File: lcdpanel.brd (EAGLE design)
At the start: 90 x 65 mm, 28 parts, among them CON1 AVRISP-NEWSYMBOL-ML6, J1 CHARLCD-LONG, SW1 PUSHSW, SW2 PUSHSW, SW3 PUSHSW, SW4 PUSHSW, U1 ATTINY2313P

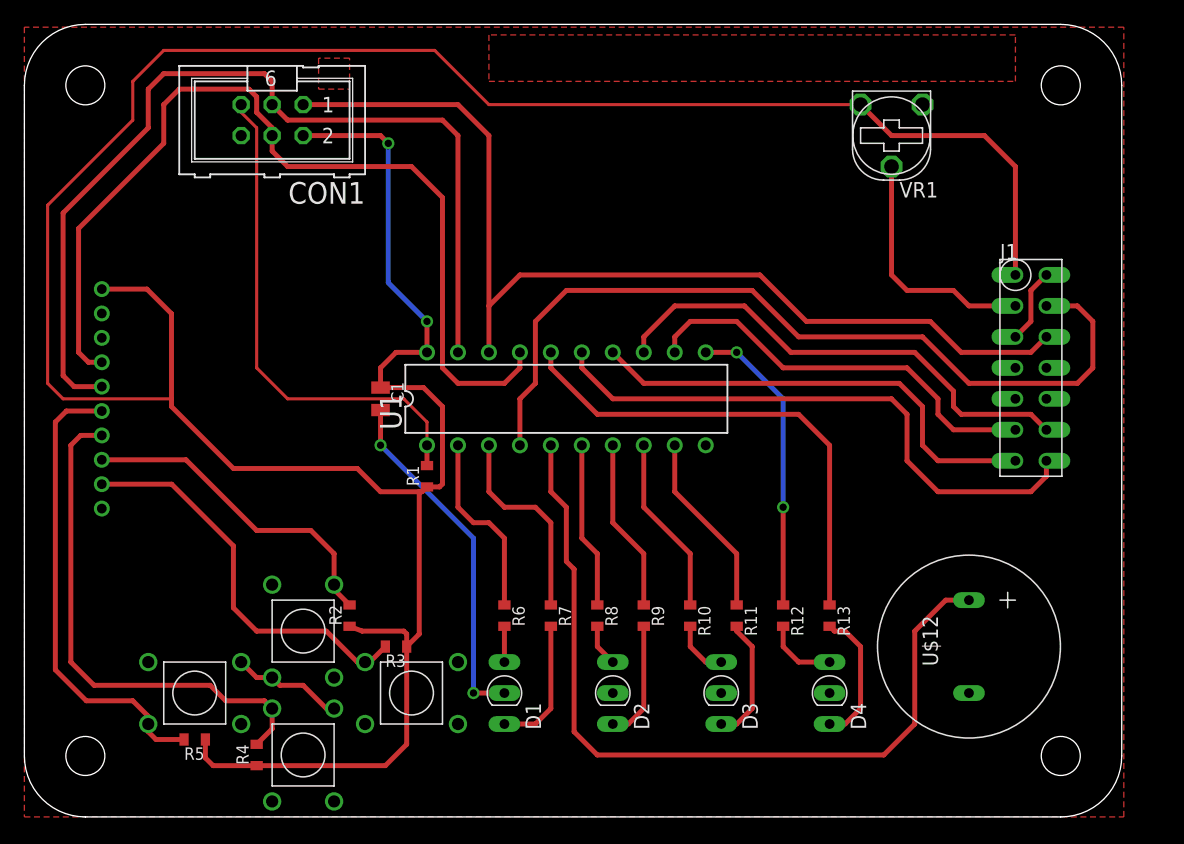
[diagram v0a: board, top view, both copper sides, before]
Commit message: added top board (ontheway)
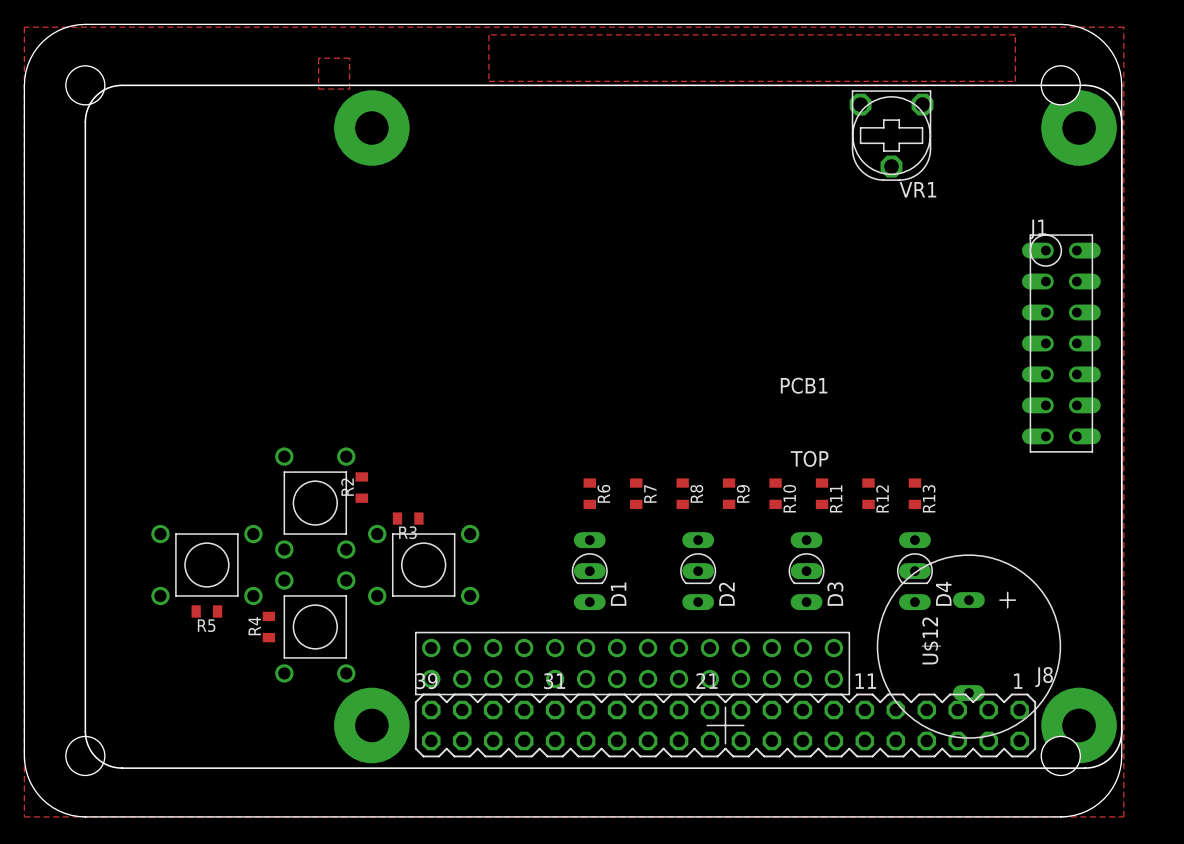
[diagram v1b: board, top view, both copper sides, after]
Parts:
- removed C1: 0.1u, Passive_Robotech:2012-C
- removed CON1: AVRISP-NEWSYMBOL-ML6, Connector_Robotech:ML6
- removed R1: 10k, Passive_Robotech:1608
- removed S1: 10B-PH, con-jst:S10B-PH
- removed U1: ATTINY2313P, MicroControler_Robotech:DIL20
- added PCB1: RASPBERRY_PI_B+, RASPBERRY_PI_Bplus:RASPBERRY_PI_B+
- added U$13: CON_14X2, pizaid:CON_14X2
- moved D3 12.2 mm to (64.2, 20.2)
- moved R12 12.2 mm to (69.2, 26.5)
- moved D1 12.2 mm to (46.4, 20.2)
- moved D2 12.2 mm to (55.3, 20.2)
- moved D4 12.2 mm to (73.0, 20.2)
- moved R10 12.2 mm to (61.6, 26.5)
- moved R11 12.2 mm to (65.4, 26.5)
- moved R13 12.2 mm to (73.0, 26.5)
- moved R6 12.2 mm to (46.4, 26.5)
- moved R7 12.2 mm to (50.2, 26.5)
- moved R8 12.2 mm to (54.0, 26.5)
- moved R9 12.2 mm to (57.8, 26.5)
- moved R5 10.5 mm to (15.0, 16.9)
- moved R2 10.5 mm to (27.7, 27.0)
- moved R4 10.5 mm to (20.1, 15.6)
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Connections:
- removed net +3V3: S1.P$2
- removed net N$12: R6.1, U1.2
- removed net N$13: R7.1, U1.3
- removed net N$14: R8.1, U1.6
- removed net N$15: R9.1, U1.7
- removed net N$16: R10.1, U1.8
- removed net N$17: R11.1, U1.9
- removed net N$18: R12.1, U1.11
- removed net N$19: R13.1, U1.16
- removed net N$20: U$12.+, U1.5
- removed net SCL: CON1.3, S1.P$5, U1.19
- removed net SDA: CON1.4, S1.P$4, U1.17
- new net LED1G: R6.1
- net +5V: now also U$13.P$5; no longer C1.1, CON1.2, R1.1, S1.P$1, U1.20
- net DB4: now also U$13.P$28; no longer U1.12
- net DB5: now also U$13.P$26; no longer U1.13
- net DB6: now also U$13.P$24; no longer U1.14
- net DB7: now also U$13.P$20; no longer U1.15
- net D_BUTTON: no longer S1.P$7
- net E: now also U$13.P$16; no longer CON1.1, U1.18
- net GND: now also U$12.+, U$13.P$13, U$13.P$18, U$13.P$2, U$13.P$22, U$13.P$27, U$13.P$8; no longer C1.2, CON1.6, S1.P$3, U$12.-, U1.10
- net L_BUTTON: no longer S1.P$6
- net N$1: now also U$12.-, U$13.P$10; no longer CON1.5, R1.2, U1.1
- net RS: now also U$13.P$14; no longer U1.4
- net R_BUTTON: no longer S1.P$9
- net U_BUTTON: no longer S1.P$8
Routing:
- net +5V: track 253.9 -> 0.00 mm, vias 2 -> 0
- net E: track 84.0 -> 0.00 mm
- net SDA: track 77.0 -> 0.00 mm
- net SCL: track 76.9 -> 0.00 mm
- net RS: track 69.3 -> 0.00 mm
- net N$20: track 67.2 -> 0.00 mm
- net DB7: track 47.6 -> 0.00 mm
- net D_BUTTON: track 42.2 -> 0.00 mm
- net N$1: track 41.5 -> 0.00 mm
- net DB5: track 40.3 -> 0.00 mm
- net N$19: track 39.9 -> 0.00 mm
- net DB6: track 38.6 -> 0.00 mm
- net L_BUTTON: track 38.2 -> 0.00 mm
- net GND: track 35.0 -> 0.00 mm, vias 2 -> 0
- net DB4: track 34.2 -> 0.00 mm
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
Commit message: continuing placement.....................
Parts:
- added U$11, U$2, U$3, U$4: B2P-VH, pizaid:B2P-VH
- added U$14: CON_14X2, pizaid:CON_14X2
- added X1: DCJACK-MJ179P-R, kamiki-dcjack:MJ-179P-R
- moved SW3 49.4 mm to (71.0, 52.0)
- moved SW4 48.9 mm to (60.5, 48.0), turned to 90 degrees
- moved SW1 47.2 mm to (60.5, 55.5), turned to 90 degrees
- moved SW2 47.0 mm to (50.0, 52.0)
- moved D2 35.1 mm to (32.3, 46.7)
- moved D3 35.1 mm to (41.1, 46.7)
- moved D4 35.1 mm to (50.0, 46.7)
- moved R10 35.1 mm to (38.6, 53.0)
- moved R11 35.1 mm to (42.4, 53.0)
- moved R12 35.1 mm to (46.2, 53.0)
- moved R13 35.1 mm to (50.0, 53.0)
- moved R7 35.1 mm to (27.2, 53.0)
- moved R8 35.1 mm to (31.0, 53.0)
- moved R9 35.1 mm to (34.8, 53.0)
- moved D1 35.1 mm to (23.4, 46.7)
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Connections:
- new net 5V0@2: U$11.P$1, U$14.P$19, U$14.P$20, U$14.P$21, U$14.P$22, U$14.P$23, U$4.P$1
- new net JNET: U$14.P$10, U$14.P$11, U$14.P$12, U$14.P$13, U$14.P$9, U$2.P$1, U$3.P$1
- new net N$13: U$14.P$5, U$14.P$6, U$14.P$7, U$14.P$8, X1.1
- new net N$15: U$14.P$14, U$14.P$15, U$14.P$16, U$14.P$17, U$14.P$18, U$2.P$2, U$3.P$2
- new net N$16: U$11.P$2, U$14.P$24, U$14.P$25, U$14.P$26, U$14.P$27, U$14.P$28, U$4.P$2
- new net N$18: U$14.P$2, U$14.P$4
- new net N$19: U$14.P$1, U$14.P$3
- net GND: now also X1.2, X1.3
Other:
- board size 90 x 65 mm -> 88.6 x 65 mm

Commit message: airwireが表示されないくてよくわかんない
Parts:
- moved R5 64.9 mm to (72.9, 46.5), turned to 90 degrees
- moved R4 63.1 mm to (75.0, 46.5)
- moved R2 53.3 mm to (77.3, 46.5)
- moved R3 53.1 mm to (79.7, 46.5), turned to 90 degrees
- moved D1 14.2 mm to (37.5, 47.5), turned to 90 degrees
- moved U$12 13.9 mm to (66.8, 22.8)
- moved D2 10.3 mm to (37.5, 55.5), turned to 90 degrees
- moved D4 9.52 mm to (46.5, 55.5), turned to 90 degrees
- moved R13 6.23 mm to (56.2, 53.5)
- moved SW2 6.23 mm to (56.2, 52.5)
- moved SW1 6.23 mm to (66.7, 56.0)
- moved SW3 6.23 mm to (77.2, 52.5)
- moved SW4 6.23 mm to (66.7, 48.5)
- moved VR1 5.75 mm to (85.5, 48.9), turned to 180 degrees
- moved D3 5.42 mm to (46.5, 47.5), turned to 90 degrees
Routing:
- net RS: track 0.00 -> 58.4 mm, vias 0 -> 1
- net DB5: track 0.00 -> 57.5 mm
- net DB4: track 0.00 -> 57.5 mm
- net +5V: track 0.00 -> 54.9 mm, vias 0 -> 1
- net E: track 0.00 -> 54.3 mm, vias 0 -> 1
- net DB7: track 0.00 -> 51.6 mm
- net DB6: track 0.00 -> 51.3 mm
- net GND: track 0.00 -> 40.8 mm
- net N$1: track 0.00 -> 15.3 mm
- net N$3: track 0.00 -> 12.2 mm

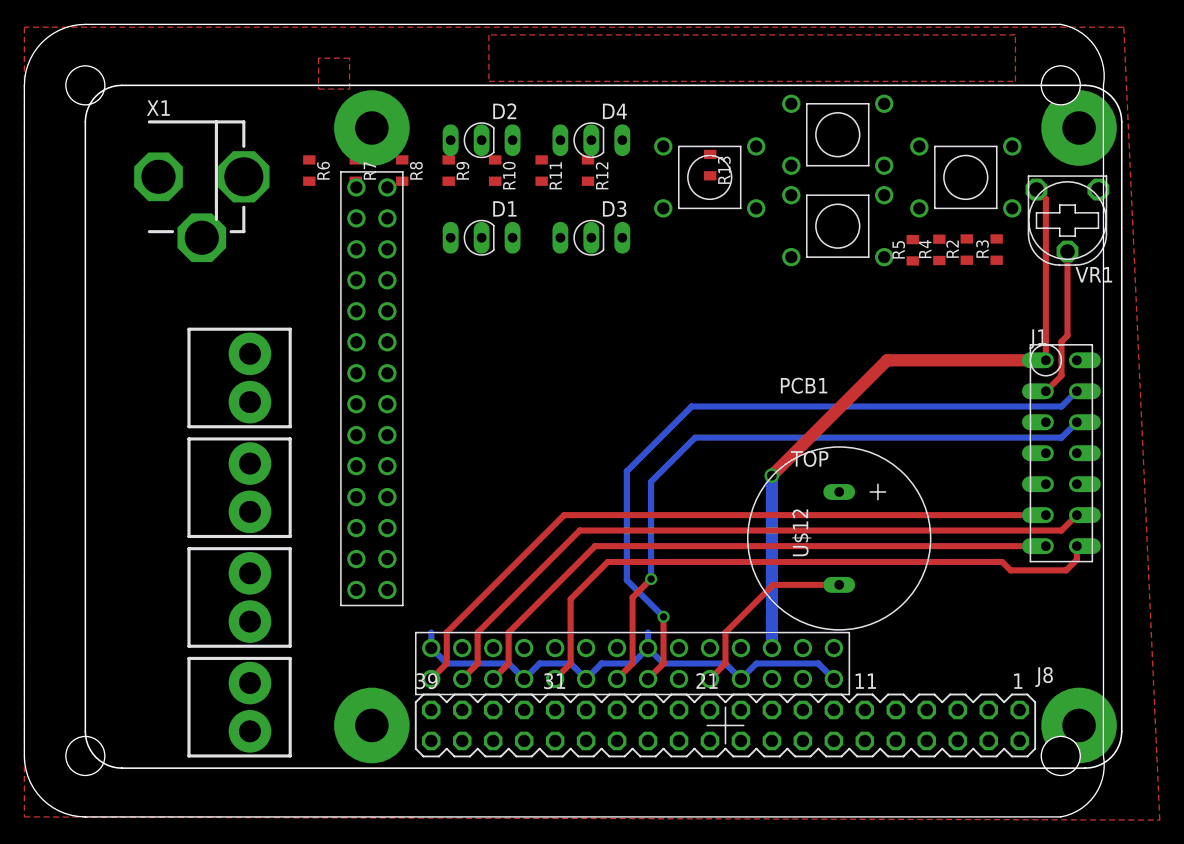
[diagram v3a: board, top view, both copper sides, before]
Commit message: draw stackable lcdpanel, not yet completed
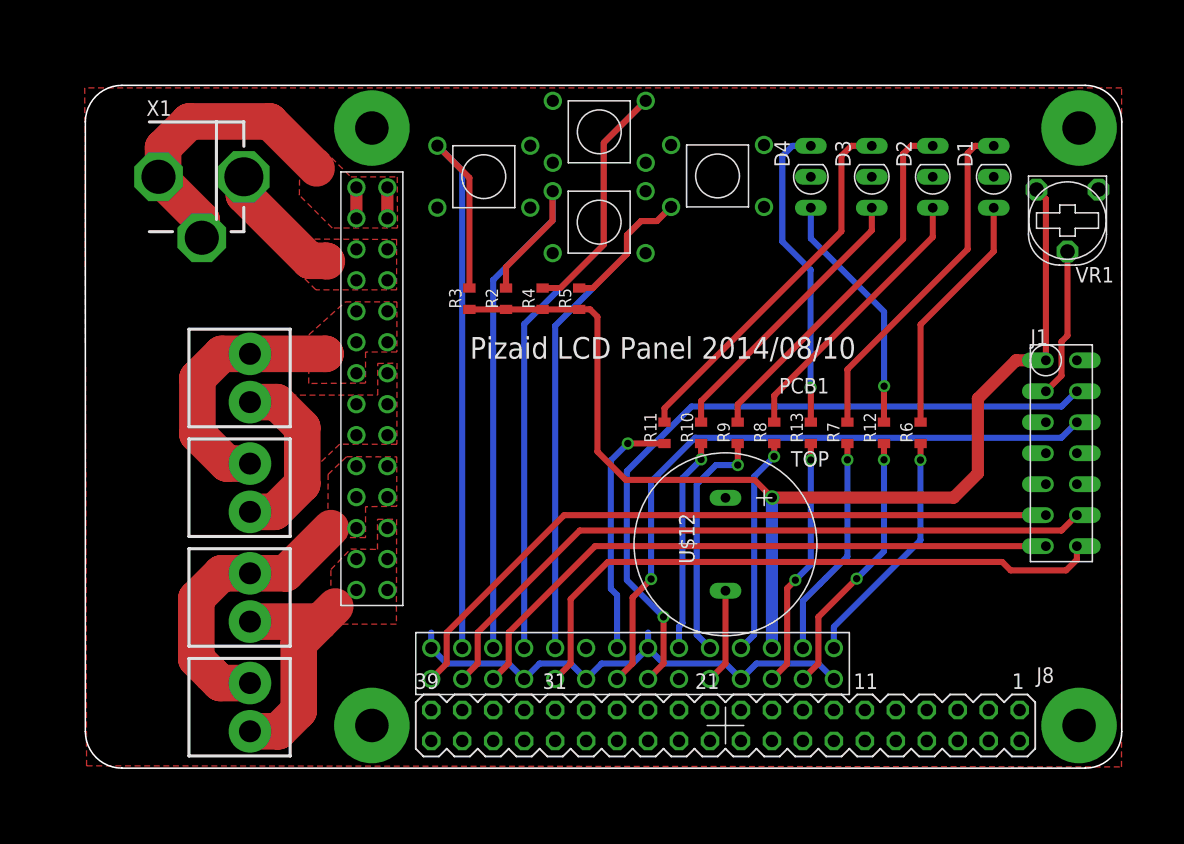
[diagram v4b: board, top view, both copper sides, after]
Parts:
- moved R6 54.5 mm to (73.5, 31.5), turned to 90 degrees
- moved R7 45.7 mm to (67.5, 31.5), turned to 90 degrees
- moved R3 43.4 mm to (36.5, 42.5)
- moved D1 42.3 mm to (79.5, 52.5), turned to 180 degrees
- moved SW3 39.5 mm to (37.7, 52.5)
- moved R2 38.0 mm to (39.5, 42.5)
- moved R8 37.3 mm to (61.5, 31.5), turned to 90 degrees
- moved D2 37.1 mm to (74.5, 52.5), turned to 180 degrees
- moved R4 32.8 mm to (42.5, 42.5)
- moved R12 32.4 mm to (70.5, 31.5), turned to 90 degrees
- moved R9 32.0 mm to (58.5, 31.5), turned to 90 degrees
- moved R5 27.6 mm to (45.5, 42.5)
- moved R10 27.3 mm to (55.5, 31.5), turned to 90 degrees
- moved R11 23.8 mm to (52.5, 31.5), turned to 90 degrees
- moved D3 23.5 mm to (69.5, 52.5), turned to 180 degrees
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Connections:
- net 5V0@2 renamed N$20
- net JNET renamed N$14
- removed net N$18: U$14.P$2, U$14.P$4
- removed net N$2: SW1.2, SW2.1, SW4.2
- new net LED1R: R7.1, U$13.P$3
- new net LED2G: R8.1, U$13.P$7
- new net LED2R: R9.1, U$13.P$9
- new net LED3G: R10.1, U$13.P$11
- new net LED3R: R11.1, U$13.P$15
- new net LED4G: R12.1, U$13.P$4
- new net LED4R: R13.1, U$13.P$6
- net D_BUTTON: now also U$13.P$21
- net GND: now also PCB1.PE_BL, PCB1.PE_BR, PCB1.PE_TL, PCB1.PE_TR, SW1.2, SW2.1; no longer X1.2, X1.3
- net LED1G: now also U$13.P$1
- net L_BUTTON: now also U$13.P$19
- net N$19: now also U$14.P$2, U$14.P$4, X1.2, X1.3
- net R_BUTTON: now also U$13.P$25
- net U_BUTTON: now also U$13.P$23
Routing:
- net D_BUTTON: track 0.00 -> 68.7 mm
- net R_BUTTON: track 0.00 -> 54.8 mm
- net L_BUTTON: track 0.00 -> 52.1 mm
- net U_BUTTON: track 0.00 -> 49.0 mm
- net +5V: track 54.9 -> 95.1 mm
- net N$8: track 0.00 -> 30.7 mm
- net N$11: track 0.00 -> 30.3 mm
- net N$19: track 0.00 -> 29.2 mm
- net N$5: track 0.00 -> 28.5 mm
- net N$10: track 0.00 -> 25.5 mm, vias 0 -> 1
- net N$20: track 0.00 -> 23.6 mm
- net N$7: track 0.00 -> 23.4 mm
- net N$6: track 0.00 -> 23.0 mm
- net LED4G: track 0.00 -> 22.1 mm, vias 0 -> 2
- net N$14: track 0.00 -> 21.2 mm
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- added copper zone on layer 1, net N$12
- added copper zone on layer 1, net N$14
- added copper zone on layer 1, net N$15
- added copper zone on layer 1, net N$16
- added copper zone on layer 1, net N$19
- added copper zone on layer 1, net N$20
- removed copper zone on layer 1, net N$21
- removed copper zone on layer 1, net N$22
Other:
- board size 88.6 x 65 mm -> 85 x 56 mm
- board text removed: "1"

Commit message: completed rev1
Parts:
- added C1, C2: (no value), rcl:C0603
- moved J1 1.81 mm to (86.7, 30.5)
- moved VR1 0.35 mm to (85.5, 49.3)
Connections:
- net +5V: now also C1.1, C2.1
- net GND: now also C1.2, C2.2
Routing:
- net +5V: track 95.1 -> 98.3 mm
- net E: track 54.3 -> 56.2 mm
- net DB5: track 57.5 -> 59.4 mm
- net DB6: track 51.3 -> 53.3 mm
- net DB4: track 57.5 -> 59.4 mm
- net N$3: track 12.2 -> 13.2 mm
- net DB7: track 51.6 -> 52.4 mm
- net RS: track 58.4 -> 59.0 mm
- net GND: vias 0 -> 39
- added copper zone on layer 16, net GND
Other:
- board text added: "Pizaid LCD Panel 2014/10/01"
- board text removed: "Pizaid LCD Panel 2014/08/10"

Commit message: fixed reversed connector on lcdpanel
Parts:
- moved R12 15.0 mm to (55.5, 31.5)
- moved R13 12.0 mm to (52.5, 31.5)
- moved R10 6.00 mm to (61.5, 31.5)
- moved R11 6.00 mm to (58.5, 31.5)
- moved R8 6.00 mm to (67.5, 31.5)
- moved R9 6.00 mm to (64.5, 31.5)
- moved R7 3.00 mm to (70.5, 31.5)
- moved U$12 1.82 mm to (55.7, 22.4)
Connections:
- net +5V: now also U$13.P$6; no longer U$13.P$5
- net DB4: now also U$13.P$26; no longer U$13.P$28
- net DB5: now also U$13.P$24; no longer U$13.P$26
- net DB6: now also U$13.P$22; no longer U$13.P$24
- net D_BUTTON: now also U$13.P$23; no longer U$13.P$21
- net E: now also U$13.P$13; no longer U$13.P$16
- net GND: now also U$13.P$1, U$13.P$14, U$13.P$17, U$13.P$21, U$13.P$28, U$13.P$7; no longer U$13.P$13, U$13.P$18, U$13.P$2, U$13.P$22, U$13.P$27, U$13.P$8
- net LED1G: now also U$13.P$2; no longer U$13.P$1
- net LED2G: now also U$13.P$4; no longer U$13.P$7
- net LED2R: now also U$13.P$5; no longer U$13.P$9
- net LED3G: now also U$13.P$8; no longer U$13.P$11
- net LED3R: now also U$13.P$9; no longer U$13.P$15
- net LED4G: now also U$13.P$11; no longer U$13.P$4
- net LED4R: now also U$13.P$12; no longer U$13.P$6
- net RS: now also U$13.P$18; no longer U$13.P$14
- net R_BUTTON: now also U$13.P$27; no longer U$13.P$25
- net U_BUTTON: now also U$13.P$25; no longer U$13.P$23
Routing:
- net GND: track 40.8 -> 0.00 mm
- net D_BUTTON: track 68.7 -> 51.7 mm, vias 0 -> 1
- net R_BUTTON: track 54.8 -> 44.6 mm, vias 0 -> 1
- net L_BUTTON: track 52.1 -> 42.0 mm, vias 0 -> 1
- net U_BUTTON: track 49.0 -> 41.4 mm, vias 0 -> 1
- net LED4G: track 22.1 -> 17.5 mm, vias 2 -> 1
- net LED2G: track 17.9 -> 21.9 mm
- net LED3G: track 17.5 -> 21.5 mm
- net +5V: track 98.3 -> 102.0 mm
- net N$10: track 25.5 -> 29.1 mm, vias 1 -> 0
- net LED1G: track 19.7 -> 22.3 mm
- net N$8: track 30.7 -> 28.2 mm
- net N$7: track 23.4 -> 20.9 mm
- net N$6: track 23.0 -> 20.5 mm
- net N$11: track 30.3 -> 27.8 mm
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
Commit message: add AVR and bug fix
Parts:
- added C3: (no value), rcl:C0603
- added CON1: AVRISP-NEWSYMBOL-ML6, Connector_Robotech:ML6
- added R1: 10k, Passive_Robotech:1608
- added U1: ATTINY2313P, MicroControler_Robotech:DIL20
- moved R13 15.2 mm to (62.5, 43.0)
- moved R12 14.9 mm to (65.0, 43.0)
- moved R11 14.6 mm to (67.5, 43.0)
- moved R10 14.3 mm to (70.0, 43.0)
- moved R9 14.0 mm to (72.5, 43.0)
- moved R8 13.7 mm to (75.0, 43.0)
- moved R7 13.5 mm to (77.5, 43.0)
- moved R6 13.2 mm to (80.0, 43.0)
- moved U$12 12.9 mm to (42.9, 23.8), turned to 0 degrees
- moved C1 5.75 mm to (81.1, 34.5), turned to 180 degrees
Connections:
- net R_BUTTON renamed MVO
- new net N$1: CON1.5, R1.2, U1.1
- new net SCL: CON1.3, U$13.P$2, U1.19
- new net SDA: CON1.4, U$13.P$3, U1.17
- net +5V: now also C3.1, CON1.2, R1.1, U1.20
- net DB4: now also U1.12; no longer U$13.P$26
- net DB5: now also U1.13; no longer U$13.P$24
- net DB6: now also U1.14; no longer U$13.P$22
- net DB7: now also U1.15; no longer U$13.P$20
- net E: now also CON1.1, U1.18; no longer U$13.P$13
- net GND: now also C3.2, CON1.6, U1.10
- net LED1G: now also U1.2; no longer U$13.P$2
- net LED1R: now also U1.3; no longer U$13.P$3
- net LED2G: now also U1.6; no longer U$13.P$4
- net LED2R: now also U1.7; no longer U$13.P$5
- net LED3G: now also U1.8; no longer U$13.P$8
- net LED3R: now also U1.9; no longer U$13.P$9
- net LED4G: now also U1.11; no longer U$13.P$11
- net LED4R: now also U1.16; no longer U$13.P$12
- net N$2: now also U1.5; no longer U$13.P$10
- net RS: now also U1.4; no longer U$13.P$18
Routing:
- net RS: track 60.6 -> 21.0 mm
- net DB6: track 53.3 -> 24.5 mm
- net DB5: track 59.4 -> 31.0 mm
- net DB4: track 59.4 -> 31.2 mm
- net DB7: track 52.4 -> 24.5 mm
- net SDA: track 0.00 -> 25.4 mm
- net N$1: track 0.00 -> 23.9 mm
- net SCL: track 0.00 -> 17.4 mm
- net N$2: track 8.12 -> 24.2 mm
- net N$10: track 29.1 -> 13.2 mm
- net N$9: track 21.3 -> 6.29 mm
- net N$8: track 28.2 -> 13.2 mm
- net N$7: track 20.9 -> 6.29 mm
- net N$11: track 27.8 -> 13.4 mm
- net N$6: track 20.5 -> 6.29 mm
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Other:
- board text added: "Pizaid LCD Panel 2014/12/20"
- board text removed: "Pizaid LCD Panel 2014/10/01"
